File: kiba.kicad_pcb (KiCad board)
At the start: 2 copper layers, 56.5 x 65 mm, 73 parts, among them IC1 TCA9548ARGERQ1, IC2 SGP40-D-R4, IC3 SGP40-D-R4, IC4 SGP40-D-R4, IC6 SGP40-D-R4, J1 Raspberry_Pi_2_3, Q1 2N7002NXAKR, U1 LM1117MP-3.3, U3 BMP581, U4 BMP581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

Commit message: feat: first pcb draft completed
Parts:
- moved JP2 43.5 mm to (132.0, 127.8)
- moved JP6 37.8 mm to (129.1, 127.8)
- moved JP7 32.3 mm to (126.2, 127.9)
- moved C7 8.09 mm to (120.3, 78.4), turned to 90 degrees
- moved C12 6.28 mm to (91.8, 95.7)
- moved R12 6.27 mm to (112.4, 77.6)
- moved R10 6.27 mm to (114.0, 77.6)
- moved R6 6.27 mm to (91.1, 100.3)
- moved R5 6.26 mm to (91.8, 94.1)
- moved R20 6.25 mm to (91.1, 101.9)
- moved C13 5.72 mm to (112.4, 124.7), turned to -90 degrees
- moved C11 5.68 mm to (106.7, 124.7), turned to 90 degrees
- moved C5 5.40 mm to (88.8, 98.0), turned to 90 degrees
- moved C18 5.39 mm to (116.3, 75.2), turned to 0 degrees
- moved C4 5.36 mm to (94.1, 98.7), turned to 90 degrees
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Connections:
- IC1 pad 10: /Sensors/SDA_PRESS_1 -> /Sensors/SDA_PRESS_4
- IC1 pad 11: /Sensors/SCK_PRESS_1 -> /Sensors/SCK_PRESS_4
- IC1 pad 12: /Sensors/SDA_PRESS_2 -> /Sensors/SDA_GAS_4
- IC1 pad 13: /Sensors/SCK_PRESS_2 -> /Sensors/SCL_GAS_4
- IC1 pad 16: /Sensors/SDA_PRESS_4 -> /Sensors/SDA_GAS_3
- IC1 pad 17: /Sensors/SCK_PRESS_4 -> /Sensors/SCL_GAS_3
- IC1 pad 3: /Sensors/SDA_GAS_2 -> /Sensors/SCK_PRESS_2
- IC1 pad 4: /Sensors/SCL_GAS_2 -> /Sensors/SDA_PRESS_2
- IC1 pad 5: /Sensors/SDA_GAS_3 -> /Sensors/SDA_GAS_2
- IC1 pad 6: /Sensors/SCL_GAS_3 -> /Sensors/SCL_GAS_2
- IC1 pad 7: /Sensors/SDA_GAS_4 -> /Sensors/SDA_PRESS_1
- IC1 pad 8: /Sensors/SCL_GAS_4 -> /Sensors/SCK_PRESS_1
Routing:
- net +3V3: track 150.3 -> 325.3 mm, vias 7 -> 23
- net /Sensors/A0: track 0.00 -> 56.9 mm, vias 0 -> 1
- net /Sensors/A1: track 0.00 -> 50.7 mm, vias 0 -> 1
- net /Sensors/SDA: track 0.00 -> 40.6 mm
- net /Sensors/SCK: track 0.00 -> 40.4 mm
- net /~{RESET}: track 0.00 -> 38.2 mm, vias 0 -> 1
- net /Sensors/SDA_GAS_1: track 1.56 -> 34.5 mm
- net /Sensors/A2: track 0.00 -> 32.7 mm, vias 0 -> 1
- net /Sensors/SCL_GAS_1: track 1.58 -> 33.7 mm
- net GND: track 6.67 -> 36.2 mm, vias 2 -> 14
- net /Sensors/SDA_PRESS_2: track 3.81 -> 32.5 mm
- net /Sensors/SCL_GAS_4: track 1.58 -> 29.9 mm
- net /Sensors/SCK_PRESS_2: track 6.24 -> 34.4 mm
- net /Sensors/SDA_GAS_2: track 1.58 -> 25.8 mm
- net /Sensors/SCL_GAS_2: track 1.58 -> 23.3 mm
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
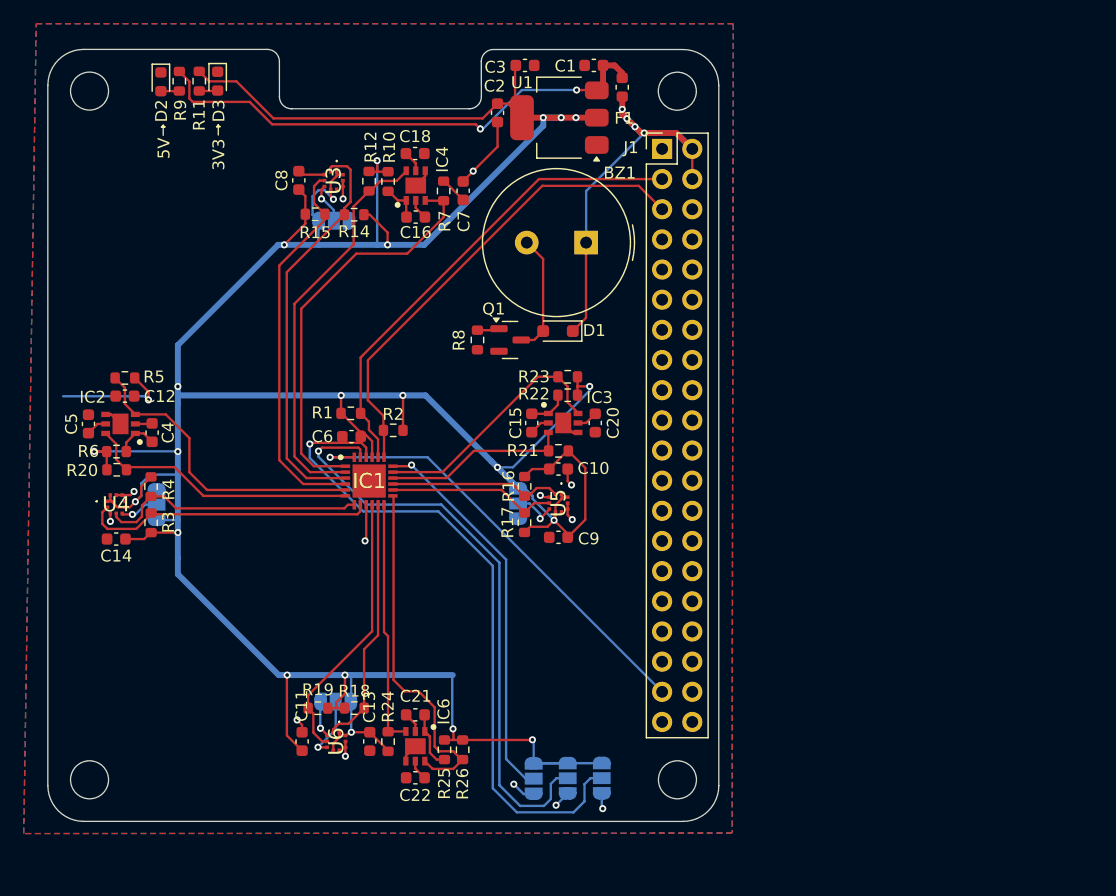
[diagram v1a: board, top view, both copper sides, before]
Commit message: fix: drc errors
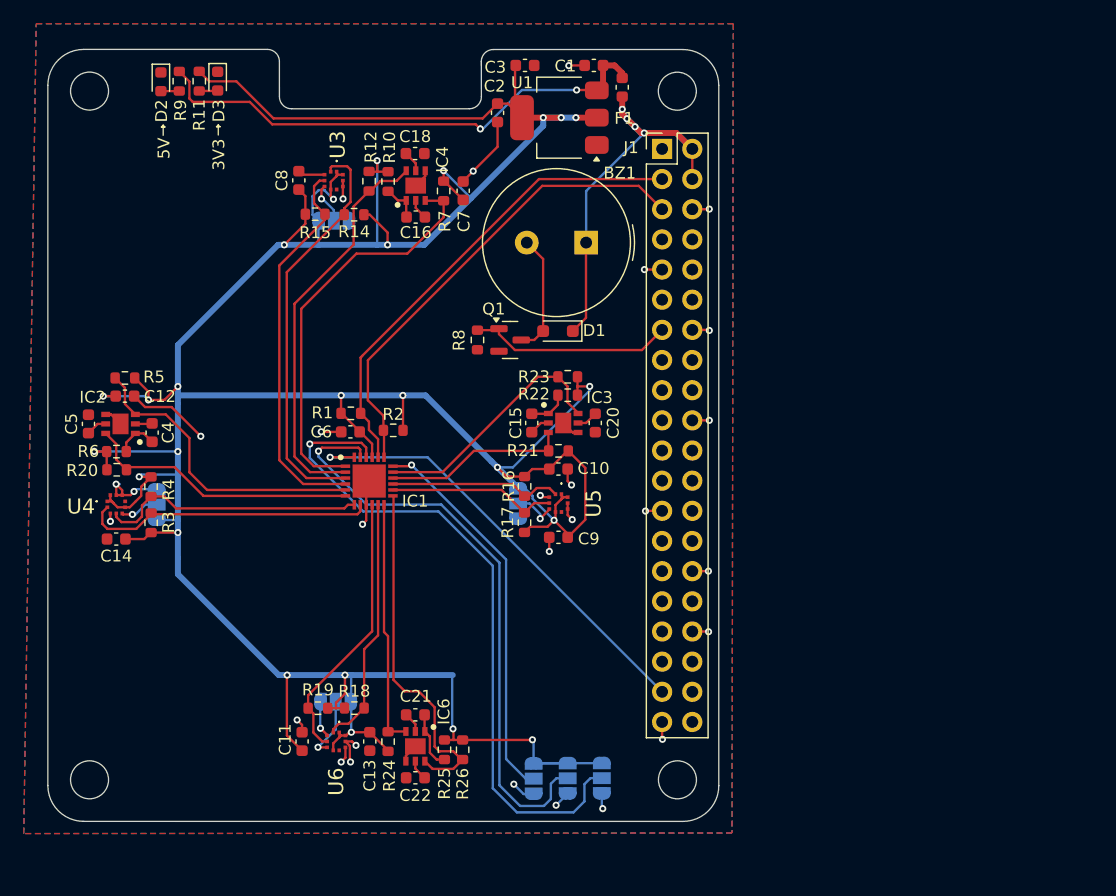
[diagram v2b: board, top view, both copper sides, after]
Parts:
- moved C6 0.41 mm to (110.8, 98.7)
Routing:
- net GND: track 36.2 -> 67.1 mm, vias 14 -> 29
- net /BUZZ: track 1.86 -> 17.3 mm
- net +3V3: track 325.3 -> 331.8 mm, vias 23 -> 25

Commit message: fix: silkscreen
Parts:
- moved C11 30.4 mm to (137.0, 128.0)
- moved JP7 30.4 mm to (156.5, 131.1)
- moved U6 30.4 mm to (139.9, 128.0)
- moved BZ1 30.4 mm to (160.9, 86.0)
- moved C1 30.4 mm to (161.6, 71.1)
- moved C12 30.4 mm to (122.1, 98.9)
- moved C13 30.4 mm to (142.7, 128.0)
- moved C16 30.4 mm to (146.6, 83.8)
- moved C20 30.4 mm to (161.7, 101.2)
- moved C21 30.4 mm to (146.5, 125.8)
- moved C22 30.4 mm to (146.5, 131.1)
- moved C4 30.4 mm to (124.4, 102.0)
- moved C5 30.4 mm to (119.0, 101.2)
- moved C6 30.4 mm to (141.1, 101.9)
- moved C7 30.4 mm to (150.6, 81.6)
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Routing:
- net GND: vias 29 -> 30
